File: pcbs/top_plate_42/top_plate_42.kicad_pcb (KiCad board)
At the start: 2 copper layers, 140.4 x 101.6 mm, 5 parts

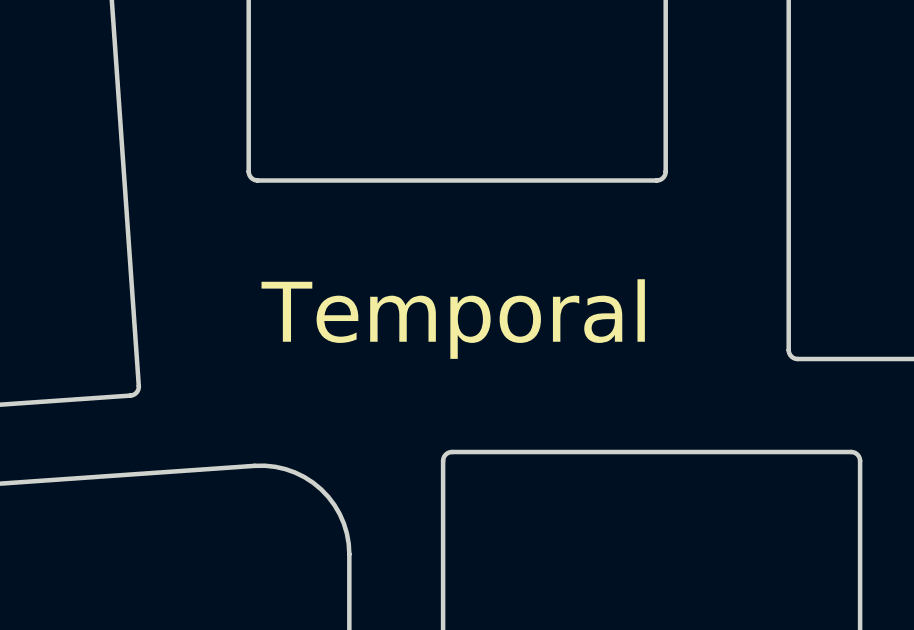
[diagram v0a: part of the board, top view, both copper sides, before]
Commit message: Add choc v2 support, KiCad 10 compatibility, and solid via zone connections
- Union choc v1/v2 switch footprint with reworked S11 trace topology
- Fix three KiCad 9->10 API breaks (zone fill setter rename, board
  outline signature, lexicographic Version() comparison that silently
  produced zero stitching vias)
- Add custom DRC rules (.kicad_dru) forcing solid zone connections for
  vias, clearing 5 copper slivers and 2 dangling vias
- Enlarge Temporal and MCU silkscreen text so substituted font weights
  meet the thickness minimum
- Make `make deps` work on Linux; patch xmldom vulnerability via override

Co-Authored-By: Claude Opus 5 <noreply@anthropic.com>
Claude-Session: https://claude.ai/code/session_0194GVHaar7of28HBuMhMdgC
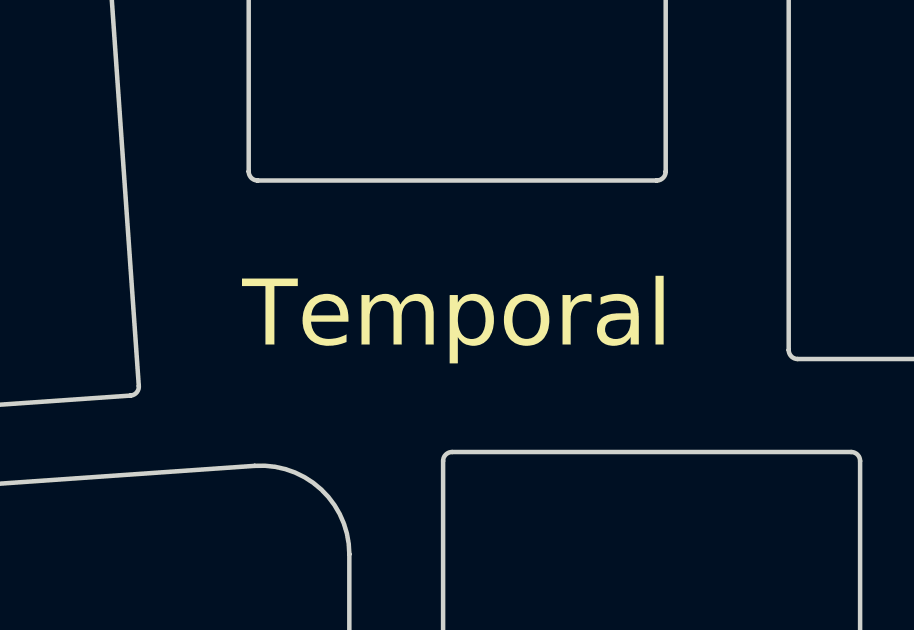
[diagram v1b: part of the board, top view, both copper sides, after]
